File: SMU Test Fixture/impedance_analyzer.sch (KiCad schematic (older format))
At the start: 9 parts, among them K2 EC2-12SNU, K3 EC2-12SNU, K4 EC2-12SNU

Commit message: Footprint updates
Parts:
- R1: footprint (none) -> Resistor_SMD:R_1206_3216Metric_Pad1.30x1.75mm_HandSolder; PN (none) -> RG3216N-1004-W-T1
- R2: footprint (none) -> Resistor_SMD:R_0805_2012Metric_Pad1.20x1.40mm_HandSolder; PN (none) -> RG2012N-104-W-T1
- R3: footprint (none) -> Resistor_SMD:R_0805_2012Metric_Pad1.20x1.40mm_HandSolder; PN (none) -> RG2012N-103-W-T1
- R4: footprint (none) -> Resistor_SMD:R_0805_2012Metric_Pad1.20x1.40mm_HandSolder; PN (none) -> RG2012N-102-W-T1
- R5: footprint (none) -> Resistor_SMD:R_0805_2012Metric_Pad1.20x1.40mm_HandSolder; PN (none) -> RG2012N-101-W-T1
- R6: footprint (none) -> Resistor_SMD:R_0805_2012Metric_Pad1.20x1.40mm_HandSolder; PN (none) -> RQ73C2A10RBTDF
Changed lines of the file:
@@
 F 0 "R2" V 7500 3475 50  0000 C CNN
 F 1 "100K" V 7550 3275 50  0000 C CNN
-F 2 "" H 7600 3475 50  0001 C CNN
+F 2 "Resistor_SMD:R_0805_2012Metric_Pad1.20x1.40mm_HandSolder" H 7600 3475 50  0001 C CNN
 F 3 "~" H 7600 3475 50  0001 C CNN
+F 4 " RG2012N-104-W-T1 " V 7600 3475 50  0001 C CNN "PN"
 	1    7600 3475
 	0    1    1    0
@@
 F 0 "R6" V 7500 4325 50  0000 C CNN
 F 1 "10R" V 7550 4175 50  0000 C CNN
-F 2 "" H 7600 4325 50  0001 C CNN
+F 2 "Resistor_SMD:R_0805_2012Metric_Pad1.20x1.40mm_HandSolder" H 7600 4325 50  0001 C CNN
 F 3 "~" H 7600 4325 50  0001 C CNN
+F 4 " RQ73C2A10RBTDF" V 7600 4325 50  0001 C CNN "PN"
 	1    7600 4325
 	0    1    1    0
@@
 F 0 "R3" V 7500 3675 50  0000 C CNN
 F 1 "10K" V 7550 3525 50  0000 C CNN
-F 2 "" H 7600 3675 50  0001 C CNN
+F 2 "Resistor_SMD:R_0805_2012Metric_Pad1.20x1.40mm_HandSolder" H 7600 3675 50  0001 C CNN
 F 3 "~" H 7600 3675 50  0001 C CNN
+F 4 " RG2012N-103-W-T1 " V 7600 3675 50  0001 C CNN "PN"
 	1    7600 3675
 	0    1    1    0
@@
 F 0 "R4" V 7500 3875 50  0000 C CNN
 F 1 "1K" V 7550 3725 50  0000 C CNN
-F 2 "" H 7600 3875 50  0001 C CNN
+F 2 "Resistor_SMD:R_0805_2012Metric_Pad1.20x1.40mm_HandSolder" H 7600 3875 50  0001 C CNN
 F 3 "~" H 7600 3875 50  0001 C CNN
+F 4 "  RG2012N-102-W-T1 " V 7600 3875 50  0001 C CNN "PN"
 	1    7600 3875
 	0    1    1    0
@@
 F 0 "R5" V 7500 4125 50  0000 C CNN
 F 1 "100R" V 7550 3925 50  0000 C CNN
-F 2 "" H 7600 4125 50  0001 C CNN
+F 2 "Resistor_SMD:R_0805_2012Metric_Pad1.20x1.40mm_HandSolder" H 7600 4125 50  0001 C CNN
 F 3 "~" H 7600 4125 50  0001 C CNN
+F 4 " RG2012N-101-W-T1 " V 7600 4125 50  0001 C CNN "PN"
 	1    7600 4125
 	0    1    1    0
@@
 F 0 "R1" V 7500 3275 50  0000 C CNN
 F 1 "1M" V 7550 3125 50  0000 C CNN
-F 2 "" H 7600 3275 50  0001 C CNN
+F 2 "Resistor_SMD:R_1206_3216Metric_Pad1.30x1.75mm_HandSolder" H 7600 3275 50  0001 C CNN
 F 3 "~" H 7600 3275 50  0001 C CNN
+F 4 " RG3216N-1004-W-T1" V 7600 3275 50  0001 C CNN "PN"
 	1    7600 3275
 	0    1    1    0

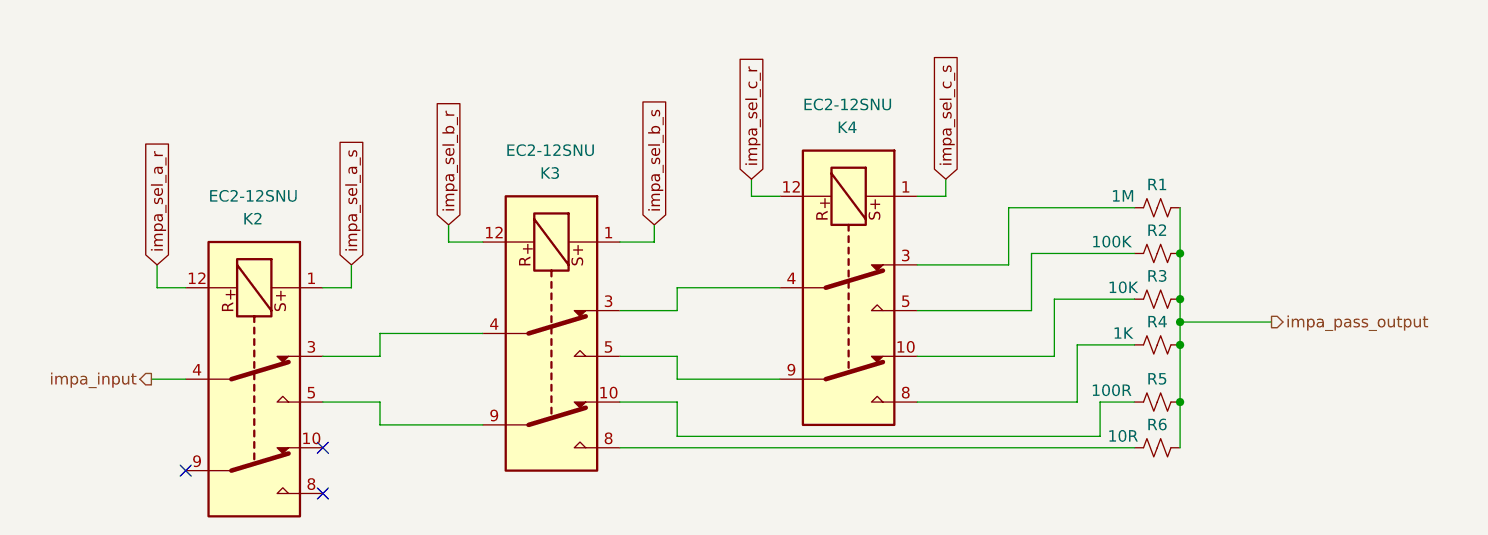
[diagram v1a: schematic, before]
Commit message: Switch to 28V txfrmr, nix preregs, nix 5V for AD2, switch to 12V relay power.
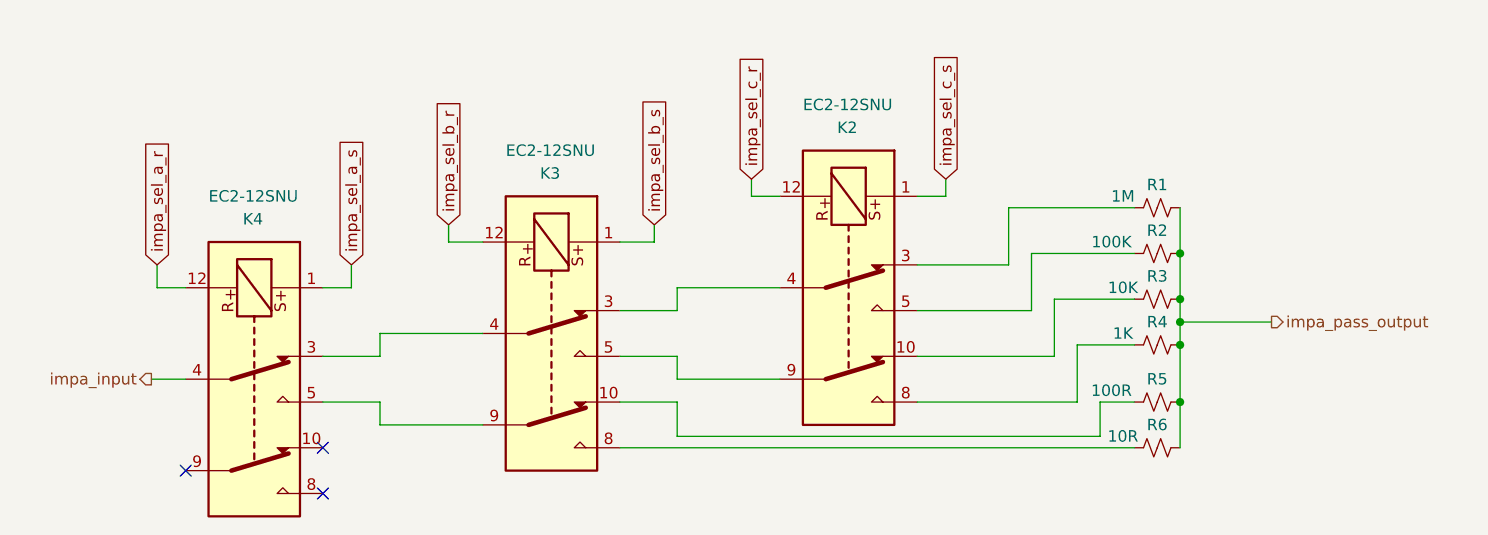
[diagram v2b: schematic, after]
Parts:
- renumbered K4 to K2, K2 to K4
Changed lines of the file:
@@
 P 3650 4025
 AR Path="/600C9795/60301A04" Ref="K?"  Part="1"
-AR Path="/5FDB00F9/60301A04" Ref="K2"  Part="1"
-F 0 "K2" V 2950 3975 50  0000 L CNN
+AR Path="/5FDB00F9/60301A04" Ref="K4"  Part="1"
+F 0 "K4" V 2950 3975 50  0000 L CNN
 F 1 "EC2-12SNU" V 2850 3825 50  0000 L CNN
 F 2 "Relay_SMD:Relay_DPDT_Kemet_EE2_NUH" H 3650 4025 50  0001 C CNN
@@
 P 6250 3625
 AR Path="/600C9795/60305373" Ref="K?"  Part="1"
-AR Path="/5FDB00F9/60305373" Ref="K4"  Part="1"
-F 0 "K4" V 5550 3575 50  0000 L CNN
+AR Path="/5FDB00F9/60305373" Ref="K2"  Part="1"
+F 0 "K2" V 5550 3575 50  0000 L CNN
 F 1 "EC2-12SNU" V 5450 3425 50  0000 L CNN
 F 2 "Relay_SMD:Relay_DPDT_Kemet_EE2_NUH" H 6250 3625 50  0001 C CNN
